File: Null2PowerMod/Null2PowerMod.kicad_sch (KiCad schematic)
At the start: 33 parts, among them J1 USB_C_Receptacle_USB2.0, J2 Conn_01x02_Female, J3 Conn_01x08, J4 Conn_01x01, J5 Conn_01x01, U1 MCP73871, U2 TPS61030PWP, U3 MMUN2133LT1G

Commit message: Major part overhaul
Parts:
- removed L1: 6.8μH, VLC5045:VLC5045T-4R7M, symbol Device:L
- removed TH1: 15K, Libraries:THRMC1005X55N, symbol Device:Thermistor
- removed U2: TPS61030PWP, TPS61030PWP:TPS61030PWP, symbol TPS61030PWP:TPS61030PWP
- added L2: VLC5045T-330M, ul_VLC5045T-330M:VLC5045T-330M, symbol ul_VLC5045T-330M:VLC5045T-330M
- added RT?: NCP15XW153J03RC, THRMC1005X55N, symbol NCP15XW153J03RC:NCP15XW153J03RC
- added U2: TPS61030PWP, PWP0016K_N, symbol ul_TPS61030PWP:TPS61030PWP
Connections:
- net +5V: now also U2.13 (VOUT), U2.14 (VOUT), U2.15 (VOUT)
- net Enable: now also U2.9 (EN)
- net GND: now also RT?.2, U2.11 (GND), U2.17 (PAD), U2.3 (PGND), U2.4 (PGND), U2.5 (PGND), U2.8 (SYNC)
- net LB0: now also U2.10 (LBO)
- net VBAT: now also L2.1, U2.6 (VBAT)
- net at R10.2, R11.1: now also U2.12 (FB)
- net at R8.2, R9.1: now also U2.7 (LBI)
- net at U1.5 (THERM): now also RT?.1
- new net: L2.2, U2.1 (SW), U2.2 (SW)

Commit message: Refreshed ideas for next milestone
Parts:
- removed C5: 0.1μF, Capacitor_SMD:C_0201_0603Metric, symbol Device:C
- removed L2: VLC5045T-330M, ul_VLC5045T-330M:VLC5045T-330M, symbol ul_VLC5045T-330M:VLC5045T-330M
- removed R10: 340k, Resistor_SMD:R_0201_0603Metric, symbol Device:R
- removed R11: 1.07MΩ, Resistor_SMD:R_0201_0603Metric, symbol Device:R
- removed R7: 1K, Resistor_SMD:R_0201_0603Metric, symbol Device:R
- removed R8: 100k, Resistor_SMD:R_0201_0603Metric, symbol Device:R
- removed R9: 1.87M, Resistor_SMD:R_0201_0603Metric, symbol Device:R
- removed U2: TPS61030PWP, PWP0016K_N, symbol ul_TPS61030PWP:TPS61030PWP
- removed U3: MMUN2133LT1G, MMUN2133LT1G:MMUN2133LT1G, symbol 2022-03-19_03-31-40:MMUN2133LT1G
- added C2: 10μF, Capacitor_SMD:C_0201_0603Metric, symbol Device:C
- added L1: VLC5045T-330M, ul_VLC5045T-330M:VLC5045T-330M, symbol ul_VLC5045T-330M:VLC5045T-330M
- added NT1: NetTie_2, NetTie:NetTie-2_SMD_Pad0.5mm, symbol Device:NetTie_2
- added R1, R2: 390kΩ, Resistor_SMD:R_0201_0603Metric, symbol Device:R
- added R3: 1.05MΩ, Resistor_SMD:R_0201_0603Metric, symbol Device:R
- added R4: 180kΩ, Resistor_SMD:R_0201_0603Metric, symbol Device:R
- added R5: 1MΩ, Resistor_SMD:R_0201_0603Metric, symbol Device:R
- added U1: TPS61030PWP, ul_TPS61030PWP:TPS61030PWP, symbol ul_TPS61030PWP:TPS61030PWP
- added U2: MMUN2133LT1G, ul_MMUN2133LT1G:MMUN2133LT1G, symbol ul_MMUN2133LT1G:MMUN2133LT1G
- C3: value 100μF -> 2.2 μF
- C4: value 10μF -> 220μF; footprint Capacitor_SMD:C_0201_0603Metric -> Capacitor_Tantalum_SMD:CP_EIA-2012-15_AVX-P
- RT1: renamed from RT?; footprint THRMC1005X55N -> NCP15XW153J03RC:THRMC1005X55N
- renumbered C6 to C5, C2 to C6, D3 to D1, D4 to D2, D1 to D3, D2 to D4, J3 to J2, J4 to J3, J5 to J4, J2 to J5, R3 to R10, R4 to R11, R5 to R12, R6 to R13, R12 to R6, R13 to R7, R1 to R8, R2 to R9, U1 to U3
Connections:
- net +5V: now also C3.1, C4.1, R3.1, R5.1, U1.13 (VOUT), U1.14 (VOUT), U1.15 (VOUT)
- net GND: now also C2.2, NT1.1, NT1.2, R2.2, R4.2, U1.11 (GND), U1.17 (PAD), U1.3 (PGND), U1.4 (PGND), U1.5 (PGND), U1.8 (SYNC)
- net LB0: now also R5.2, U1.10 (LBO), U2.1
- net at R7.1: now also U2.2
- removed net VBAT: C3.1, C4.1, J2.3 (Pin_3), U3.1 (OUT), U3.20 (OUT)
- new net: L1.2, U1.1 (SW), U1.2 (SW)
- new net: R3.2, R4.1, U1.12 (FB)
- new net: C2.1, L1.1, R1.1, U1.6 (VBAT), U1.9 (EN)
- new net: R1.2, R2.1, U1.7 (LBI)
- new net: U3.1 (OUT), U3.20 (OUT)

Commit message: Redesigning pcb
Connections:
- net Enable: now also C2.1, L1.1, R1.1, U1.6 (VBAT), U1.9 (EN)
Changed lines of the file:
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@@
   (junction (at 68.58 110.49) (diameter 0) (color 0 0 0 0)
+  )
+  (junction (at 54.61 132.08) (diameter 0) (color 0 0 0 0)
   )
   (junction (at 49.53 142.24) (diameter 0) (color 0 0 0 0)
@@
     (stroke (width 0) (type default) (color 0 0 0 0))
   )
+  (wire (pts (xy 54.61 132.08) (xy 54.61 134.62))
+    (stroke (width 0) (type default) (color 0 0 0 0))
+  )
   (wire (pts (xy 203.2 31.75) (xy 201.93 31.75))
     (stroke (width 0) (type default) (color 0 0 0 0))
@@
     (stroke (width 0) (type default) (color 0 0 0 0))
   )
+  (wire (pts (xy 40.64 132.08) (xy 54.61 132.08))
+    (stroke (width 0) (type default) (color 0 0 0 0))
+  )
   (wire (pts (xy 90.17 129.54) (xy 93.98 129.54))
     (stroke (width 0) (type default) (color 0 0 0 0))
@@
     (stroke (width 0) (type default) (color 0 0 0 0))
   )
-  (wire (pts (xy 54.61 129.54) (xy 54.61 134.62))
+  (wire (pts (xy 54.61 129.54) (xy 54.61 132.08))
     (stroke (width 0) (type default) (color 0 0 0 0))
   )
@@
     (effects (font (size 1.27 1.27)) (justify left bottom))
   )
+  (label "Enable" (at 40.64 132.08 0)
+    (effects (font (size 1.27 1.27)) (justify left bottom))
+  )

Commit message: Major revision
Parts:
- removed C3: 2.2 μF, Capacitor_SMD:C_0201_0603Metric, symbol Device:C
- removed C5: 10μF, Capacitor_SMD:C_0201_0603Metric, symbol Device:C_Polarized
- removed D1: Orange, LED_SMD:LED_0201_0603Metric, symbol Device:LED
- removed D2: RED, LED_SMD:LED_0201_0603Metric, symbol Device:LED
- removed L1: VLC5045T-330M, ul_VLC5045T-330M:VLC5045T-330M, symbol ul_VLC5045T-330M:VLC5045T-330M
- removed NT1: NetTie_2, NetTie:NetTie-2_SMD_Pad0.5mm, symbol Device:NetTie_2
- removed R6: 1k, Resistor_SMD:R_0201_0603Metric, symbol Device:R
- removed R7: 1K, Resistor_SMD:R_0201_0603Metric, symbol Device:R
- added C1: 10μF, Capacitor_SMD:C_0201_0603Metric, symbol Device:C
- added C6: 100μF, Capacitor_SMD:C_0201_0603Metric, symbol Device:C_Polarized
- added J4, J5: Conn_01x01, Connector_PinHeader_2.54mm:PinHeader_1x01_P2.54mm_Vertical, symbol Connector_Generic:Conn_01x01
- added L1: 6.8uH, ul_VLC5045T-330M:VLC5045T-330M, symbol Device:L
- added LED1: RED, LED_SMD:LED_0201_0603Metric, symbol Device:LED
- added LED2: BLUE, Capacitor_SMD:C_0201_0603Metric, symbol Device:LED
- added R13: 200k, Resistor_SMD:R_0201_0603Metric, symbol Device:R
- added R20: 1k, Resistor_SMD:R_0201_0603Metric, symbol Device:R
- C2: value 10μF -> 2.2μF
- C4: value 220μF -> 0.1μF; footprint Capacitor_Tantalum_SMD:CP_EIA-2012-15_AVX-P -> Capacitor_SMD:C_0201_0603Metric
- C8: renamed from C1; value 2.2μF -> 10μF
- CHRG/LBO1: renamed from D4; value Green -> ORANGE
- Done1: renamed from D3; value BLUE -> GREEN
- R1: value 390kΩ -> 1.87M
- R14: renamed from R12; value 200k -> 1k
- R16: renamed from R10; value 100k -> 1k
- R17: renamed from R8; value 270k -> 100k
- R2: value 390kΩ -> 340k
- R3: value 1.05MΩ -> 1.87M
- R4: value 180kΩ -> 200k
- R5: value 1MΩ -> 1k; footprint Resistor_SMD:R_0201_0603Metric -> Capacitor_SMD:C_0201_0603Metric
- R6: renamed from R11; value 200k -> 270k
- R7: renamed from R9; value 1k -> 100k
- renumbered J5 to B1, C6 to C7, J1 to CN4, J3 to J1, J4 to J3, R13 to R8, U2 to T1, RT1 to THERM1, U3 to U2
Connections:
- net +5V: now also C2.1, C6.1; no longer C4.1
- net Enable: now also R13.2; no longer C2.1, R1.1, U1.6 (VBAT)
- net GND: now also R16.2, R17.2, C1.2, C6.2, J5.1 (Pin_1), LED1.1 (K), LED2.1 (K); no longer R16.1, R17.1
- net LB0: no longer R5.2, T1.1, U1.10 (LBO)
- net VBUS: now also J4.1 (Pin_1)
- net SW: now reaches U1.1 (SW), U1.2 (SW)
- net SW: now also L1.1
- net at U2.12 (PROG3): now also R17.1; no longer R17.2
- net at U2.13 (PROG1): now also R16.1; no longer R16.2
- net at T1.2: now also R20.1
- new net: LED2.2 (A), R5.2
- new net: T1.1, U1.10 (LBO)
- new net: C1.1, C4.1, L1.2, R1.1, U1.6 (VBAT)
- new net: LED1.2 (A), R20.2
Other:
- moved on the sheet: B1, C7, CHRG/LBO1, Done1, R14, R16, R17, R6, R7, R8, T1, THERM1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

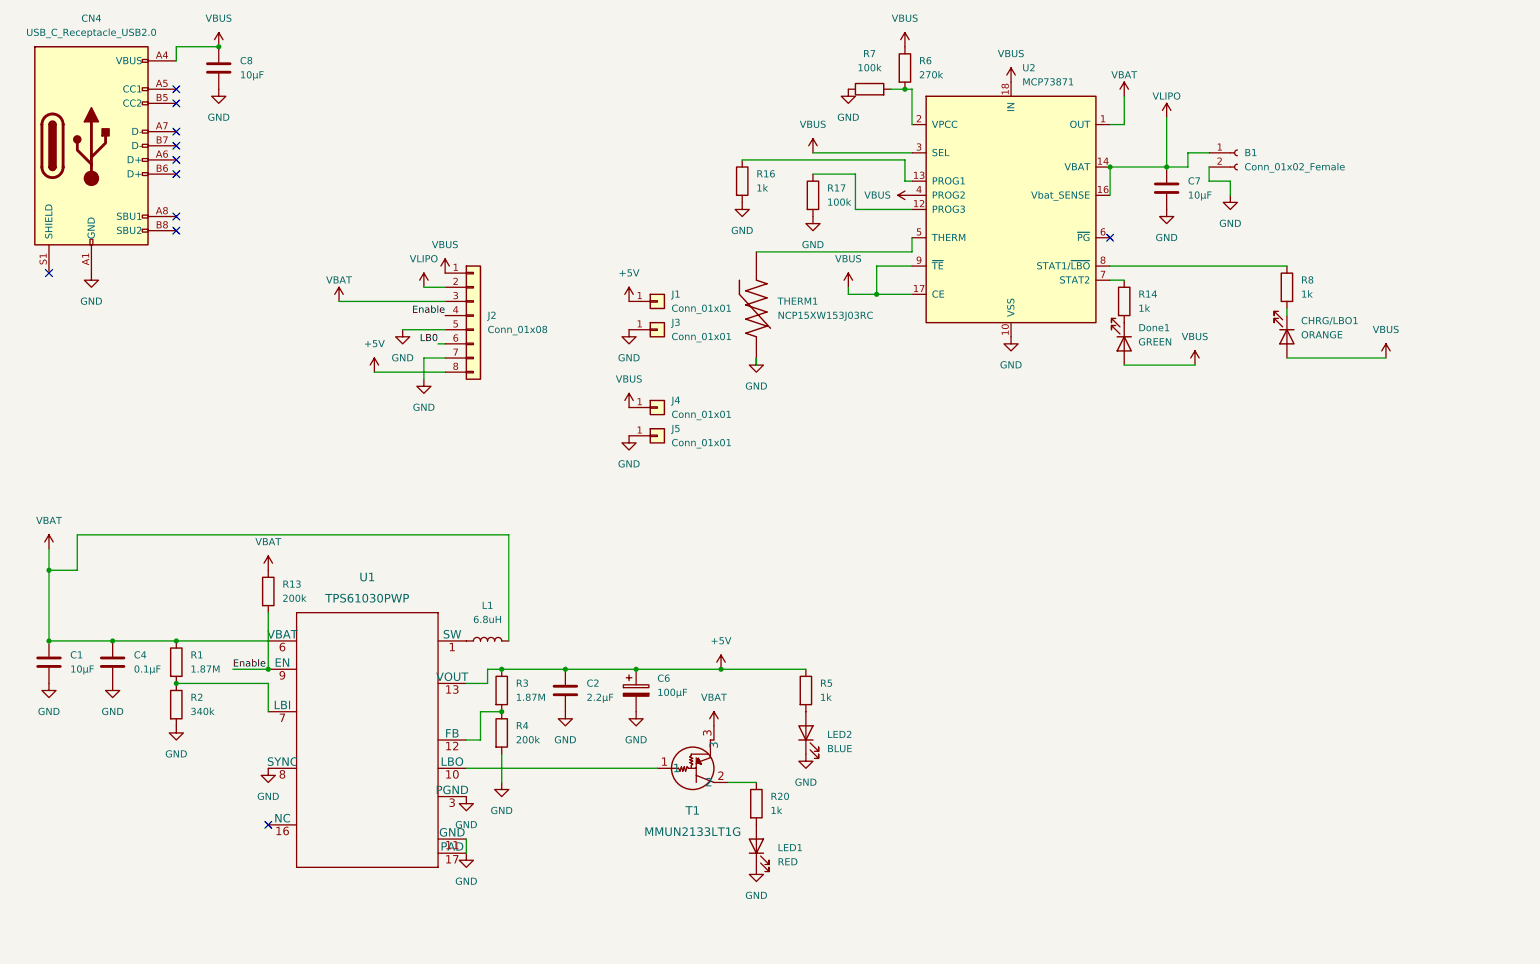
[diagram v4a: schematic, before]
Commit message: Trying out an autorouter
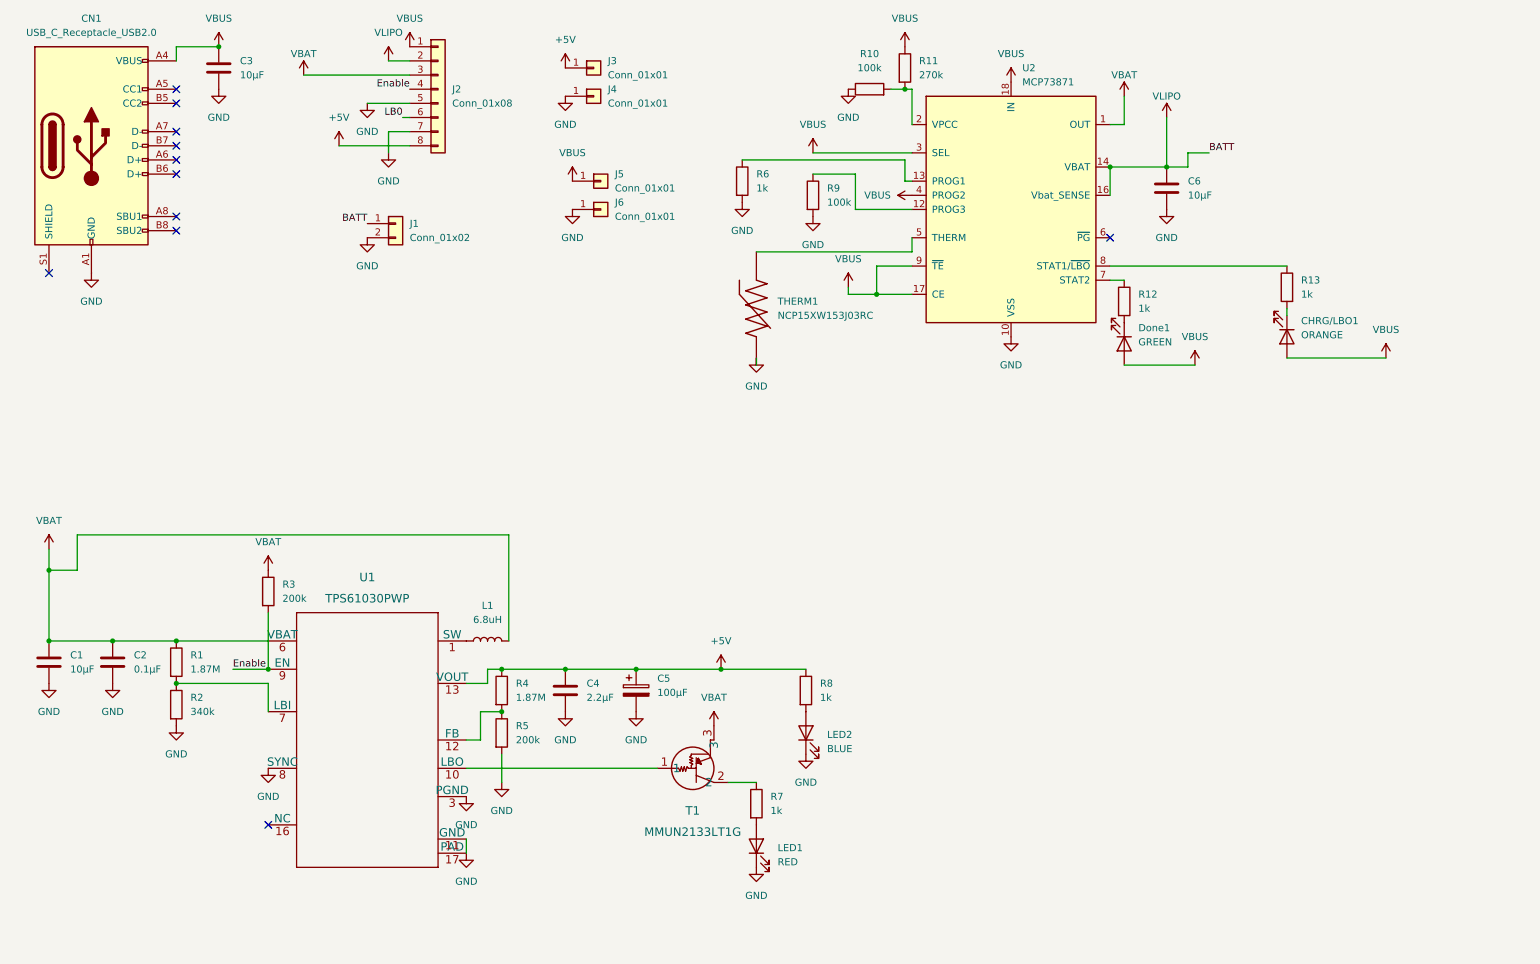
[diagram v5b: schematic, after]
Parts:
- removed B1: Conn_01x02_Female, Connector_JST:JST_EH_S2B-EH_1x02_P2.50mm_Horizontal, symbol Connector:Conn_01x02_Female
- added J1: Conn_01x02, Connector_JST:JST_EH_S2B-EH_1x02_P2.50mm_Horizontal, symbol Connector_Generic:Conn_01x02
- renumbered C4 to C2, C8 to C3, C2 to C4, C6 to C5, C7 to C6, CN4 to CN1, J1 to J3, J3 to J4, J4 to J5, J5 to J6, R7 to R10, R6 to R11, R14 to R12, R8 to R13, R13 to R3, R3 to R4, R4 to R5, R16 to R6, R20 to R7, R5 to R8, R17 to R9
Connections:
- net GND: now also J1.2 (Pin_2)
- net VLIPO: now also J1.1 (Pin_1)
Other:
- moved on the sheet: J2, J3, J4, J5, J6
